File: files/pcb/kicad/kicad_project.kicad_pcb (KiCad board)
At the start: 2 copper layers, 100 x 96 mm, 113 parts, among them CON1 USB_MINI_B, IC1 ATMEGA328-A, IC10 FET, IC11 DS1307, IC12 LPS331AP, IC13 AM2321, IC2 IC_16PIN, IC3 IC_4PIN, IC4 IC_4PIN, IC5 SN74141_K155NA, IC6 TLP627-4, IC7 TLP627-4, IC8 MY_3_TERMINAL_REGULATOR, IC9 ICM7555CD, K1 CONN_3, K2 CONN_3, K3 CONN_3, K4 CONN_3, P1 CONN_6, SW1 SW_PUSH, SW2 EVQWK, SW3 SW_PUSH, SW4 SW_PUSH, SW5 SW_PUSH, T1 2SC, T2 2SC, T3 2SA, U1 NEON, U10 NIXIE_IN_16, U11 DC_JACK, U12 LOAD, U13 remocon, U14 napion, U15 MY_PIN52, U16 MY_PIN52, U17 MY_PIN52, U18 MY_PIN52, U2 NEON, U3 NEON, U4 NEON, U5 NIXIE_IN_16, U6 NIXIE_IN_16, U7 NIXIE_IN_16, U8 NIXIE_IN_16, U9 NIXIE_IN_16, X1 12MHz, X2 32.768kHz

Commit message: PCB更新
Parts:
- moved C13 111.8 mm to (350.4, 144.9)
- moved IC10 111.8 mm to (330.2, 146.7)
- moved IC9 111.8 mm to (318.6, 142.1)
- moved L1 111.8 mm to (340.8, 144.7)
- moved T1 111.8 mm to (313.6, 148.5)
- moved T2 111.8 mm to (318.6, 148.3)
- moved T3 111.8 mm to (323.6, 148.3)
- moved VR1 111.8 mm to (311.6, 142.1)
- moved VR2 111.8 mm to (307.8, 142.1)
- moved C14 8.81 mm to (197.8, 135.3)
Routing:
- net GND: track 268.3 -> 35.8 mm, vias 11 -> 0
- net /nixie/N0: track 199.0 -> 0.00 mm, vias 10 -> 0
- net /nixie/Sheet53F9F7BA/dot_cathode_l: track 197.8 -> 0.00 mm, vias 7 -> 0
- net /nixie/N1: track 184.7 -> 0.00 mm, vias 13 -> 0
- net /nixie/N2: track 180.0 -> 0.00 mm, vias 9 -> 0
- net GND_L: track 192.4 -> 14.7 mm, vias 8 -> 0
- net +5V: track 190.2 -> 15.3 mm, vias 11 -> 1
- net /nixie/Sheet53F9F7BA/dot_cathode_r: track 140.3 -> 0.00 mm, vias 5 -> 0
- net /nixie/N9: track 124.2 -> 0.00 mm, vias 3 -> 0
- net /nixie/N8: track 107.6 -> 0.00 mm, vias 4 -> 0
- net /nixie/N7: track 105.7 -> 0.00 mm, vias 5 -> 0
- net /nixie/N4: track 104.3 -> 0.00 mm, vias 3 -> 0
- net /nixie/N3: track 100.9 -> 0.00 mm, vias 3 -> 0
- net /nixie/N6: track 96.1 -> 0.00 mm, vias 6 -> 0
- net (no net): track 95.3 -> 0.00 mm, vias 3 -> 0
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
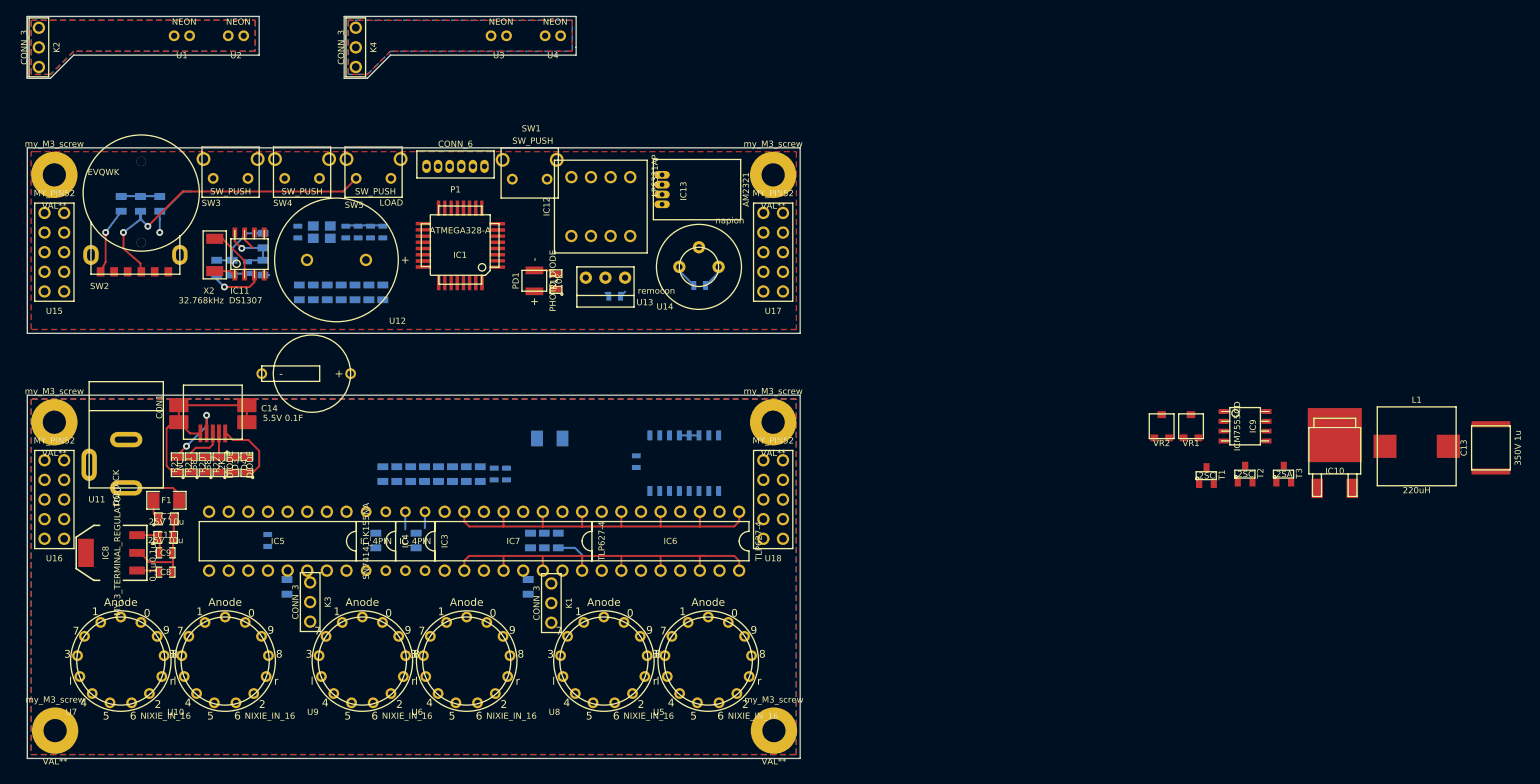
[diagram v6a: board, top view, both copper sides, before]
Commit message: 必要性の低い部品を削除
機能てんこ盛りよりシンプル小型化のほうがいいかなと思ったので一気に部品を削除
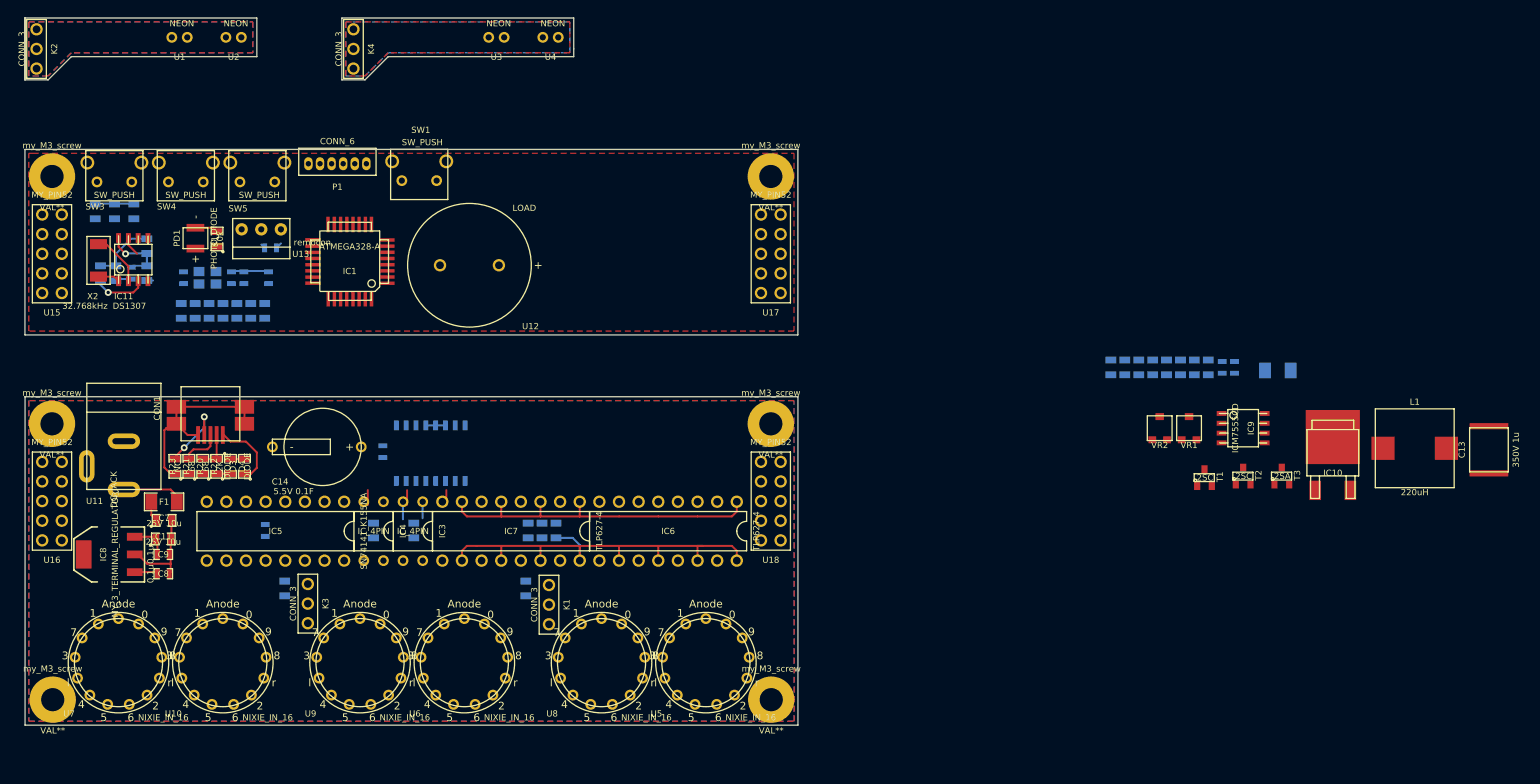
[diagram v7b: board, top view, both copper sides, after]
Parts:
- removed C17, C19: 0.1u, SM0603_Capa
- removed IC12: LPS331AP, my_dip_module
- removed IC13: AM2321, my_am2321
- removed SW2: EVQWK, my_rotary_switch
- removed U14: napion, my_napion
- moved C10 95.2 mm to (317.2, 134.5)
- moved R13 95.2 mm to (310.2, 134.5)
- moved R14 95.2 mm to (308.4, 134.5)
- moved R19 95.2 mm to (301.2, 134.5)
- moved C12 95.2 mm to (315.6, 134.5)
- moved R15 95.2 mm to (306.6, 134.5)
- moved R16 95.2 mm to (313.8, 134.5)
- moved R17 95.2 mm to (304.8, 134.5)
- moved R12 95.2 mm to (312.0, 134.5)
- moved R18 95.2 mm to (303.0, 134.5)
- moved D2 94.6 mm to (322.8, 134.9)
- moved U13 45.0 mm to (191.3, 118.9)
- moved C16 45.0 mm to (192.5, 119.0)
- moved PD1 44.2 mm to (182.8, 117.8)
- moved R11 44.2 mm to (185.6, 117.9)
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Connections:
- IC1 pad 2: /Sheet53F9209C/out -> (no net)
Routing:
- net /Sheet53F8FD69/Push: track 42.2 -> 0.00 mm, vias 2 -> 0
- net /Sheet53F8FD69/A: track 8.66 -> 0.00 mm, vias 1 -> 0
- net /Sheet53F8FD69/B: track 7.86 -> 0.00 mm, vias 1 -> 0
- net N-0000046: track 50.1 -> 44.3 mm
- net GND: track 35.8 -> 32.6 mm
- net +5V: track 15.3 -> 12.2 mm
- net /nixie/L8: track 0.00 -> 1.91 mm
- net /PB_P4: track 0.00 -> 1.91 mm
- net /PB_P3: track 1.96 -> 3.87 mm
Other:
- board size 100 x 96 mm -> 100 x 91.5 mm

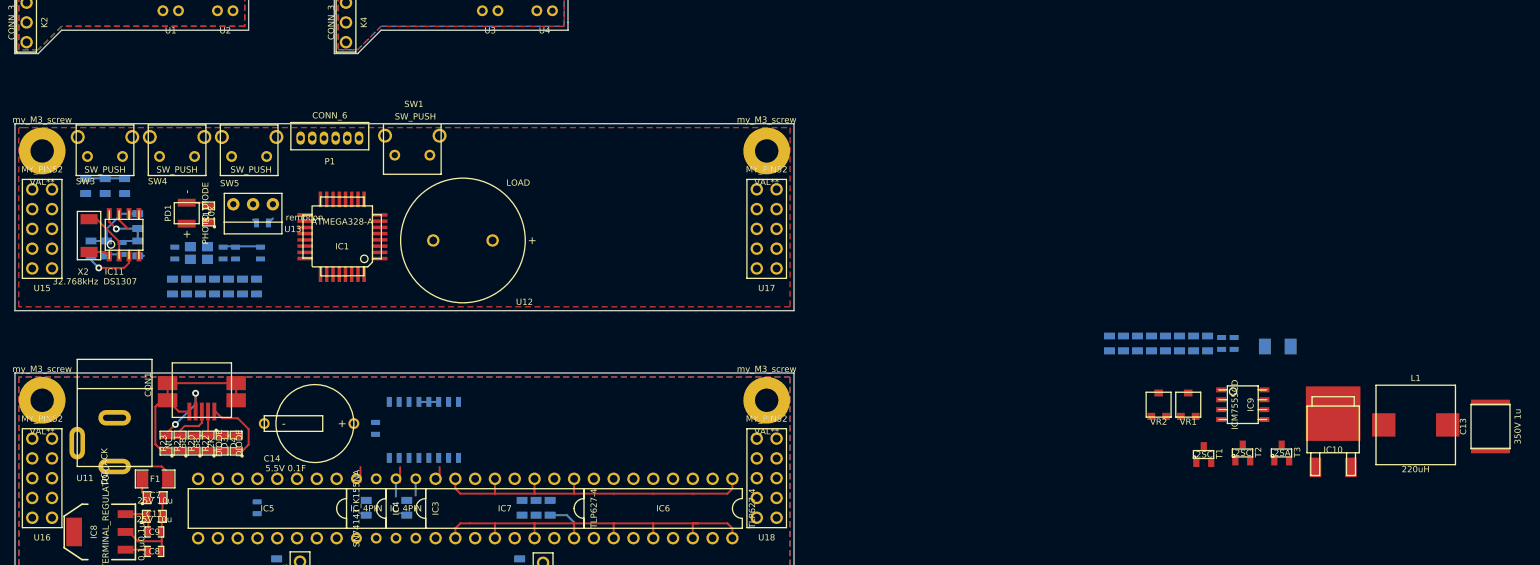
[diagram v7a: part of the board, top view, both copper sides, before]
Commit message: 設計見直し
部品見直し
USB・DCジャック自動切り替え
マイコンを下段のボードに移動
ニキシー管駆動電源を上段ボードに移動
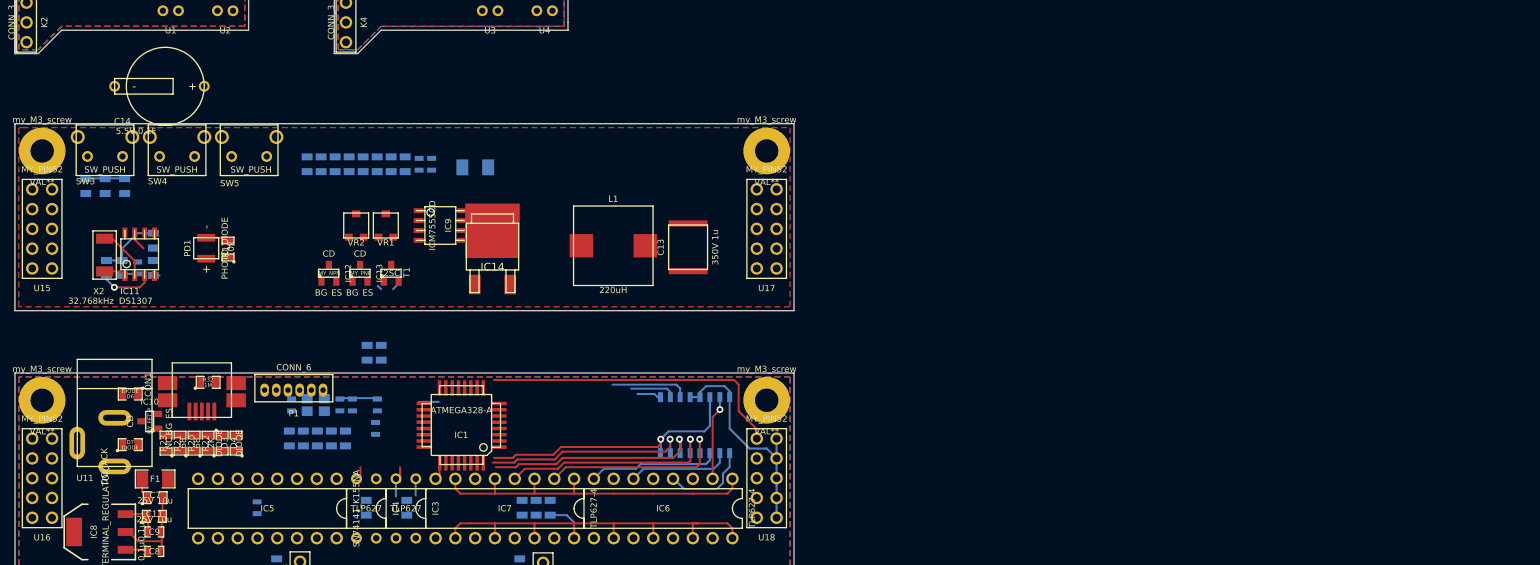
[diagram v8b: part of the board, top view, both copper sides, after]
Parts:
- removed C16: 0.1u, SM0603_Capa
- removed SW1: SW_PUSH, my_tact_switch
- removed T2: 2SC, SOT23
- removed T3: 2SA, SOT23
- removed U12: LOAD, my_sounder
- removed U13: remocon, my_remocon
- added D6: DIODE, SM0805, F.Cu at (175.5, 141.0)
- added D7: DIODE, SM0805, F.Cu at (175.5, 147.5)
- added IC12: MY_NPN, my_SOT23, F.Cu at (201.0, 125.5)
- added IC13: MY_PNP, my_SOT23, F.Cu at (205.0, 125.5)
- added IC14: MY_FET_N, my_sot428, F.Cu at (222.0, 123.5)
- added R32: 1M, SM0805, F.Cu at (185.5, 139.5)
- IC10: value FET -> MY_FET_P; footprint my_sot428 -> my_SOT23
- IC2: value IC_16PIN -> 74LC138
- IC3, IC4: value IC_4PIN -> TLP627
- moved IC10 151.9 mm to (178.0, 144.5), turned to 90 degrees
- moved T1 106.9 mm to (209.0, 125.5)
- moved C10 105.5 mm to (214.2, 111.5)
- moved R13 105.5 mm to (207.2, 111.5)
- moved R14 105.5 mm to (205.4, 111.5)
- moved R19 105.5 mm to (198.2, 111.5)
- moved C12 105.5 mm to (212.6, 111.5)
- moved C13 105.5 mm to (247.1, 122.2)
- moved D2 105.5 mm to (219.8, 111.9)
- moved R15 105.5 mm to (203.6, 111.5)
- moved R16 105.5 mm to (210.8, 111.5)
- moved R17 105.5 mm to (201.8, 111.5)
- moved IC9 105.5 mm to (215.3, 119.4)
- moved L1 105.5 mm to (237.5, 122.0)
- moved R12 105.5 mm to (209.0, 111.5)
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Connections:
- net /Sheet53F91D14/beep renamed /SCK
- C10 pad 1: GND_L -> PINGND
- C10 pad 2: N-0000078 -> PIN9V
- C11 pad 1: 5V_L -> +5V
- C11 pad 2: GND_L -> GND
- C12 pad 2: GND_L -> PINGND
- C13 pad 2: GND_L -> PINGND
- C14 pad 1: CLK_PW_L -> N-00000108
- C14 pad 2: GND -> PINGND
- C15 pad 2: GND_L -> GND
- C18 pad 1: +5V -> PIN5V
- C18 pad 2: GND -> PINGND
- C6 pad 1: GND_L -> GND
- C7 pad 1: N-0000078 -> N-0000087
- C7 pad 2: GND_L -> GND
- C8 pad 1: N-0000078 -> N-0000087
- C8 pad 2: GND_L -> GND
- C9 pad 1: 5V_L -> +5V
- C9 pad 2: GND_L -> GND
- CON1 pad 1: N-0000083 -> USB5V
- CON1 pad 2: N-0000085 -> N-00000105
- CON1 pad 3: N-0000087 -> N-00000104
- D2 pad 1: N-0000073 -> N-0000088
- D3 pad 1: N-0000084 -> GND
- D3 pad 2: +5V -> N-00000104
- D4 pad 1: N-0000083 -> GND
- D4 pad 2: N-0000084 -> N-00000105
- D5 pad 2: CLK_PW_H -> N-00000108
- F1 pad 2: N-0000078 -> N-0000087
- IC1 pad 10: /Sheet53F8FD69/B -> /PD6
- IC1 pad 11: /Sheet53F8FD69/Push -> /PD7
- IC1 pad 19: /Sheet53F8BA4D/out -> /ADC6
- IC1 pad 2: (no net) -> /PD4
- IC1 pad 27: /Sheet53F905A8/SCL -> /SDA
- IC1 pad 28: /Sheet53F905A8/SDA -> /SCL
- IC1 pad 30: /Sheet53F905A8/CLKOUT -> (no net)
- IC1 pad 31: /Sheet53F9209A/out -> (no net)
- IC1 pad 9: /Sheet53F8FD69/A -> /PD5
- IC10 pad 1: N-0000071 -> N-0000095
- IC10 pad 2: N-0000073 -> USB5V
- IC10 pad 3: GND_L -> N-0000093
- IC11 pad 3: CLK_PW_H -> N-00000108
- IC11 pad 4: GND -> PINGND
- IC11 pad 5: /Sheet53F905A8/SDA -> PINSDA
- IC11 pad 6: /Sheet53F905A8/SCL -> PINSCL
- IC11 pad 7: /Sheet53F905A8/CLKOUT -> PINCLKOUT
- IC11 pad 8: +5V -> PIN5V
- IC2 pad 1: /PB_P0 -> /PB0
- IC2 pad 2: /PB_P1 -> /PB1
- IC2 pad 3: /PB_P2 -> /PB2
- IC2 pad 4: GND_L -> GND
- IC2 pad 5: GND_L -> GND
- IC2 pad 6: GND_L -> +5V
- IC2 pad 8: GND_L -> GND
- IC3 pad 2: /PB_P3 -> /MOSI
- IC4 pad 2: /PB_P4 -> /MISO
- IC5 pad 12: GND_L -> GND
- IC5 pad 3: /PC_P3 -> /PC3
- IC5 pad 4: /PC_P2 -> /PC2
- IC5 pad 6: /PC_P1 -> /PC1
- IC5 pad 7: /PC_P0 -> /PC0
- IC8 pad 1: N-0000078 -> N-0000087
- IC8 pad 2: GND_L -> GND
- IC8 pad 3: 5V_L -> +5V
- IC9 pad 1: GND_L -> PINGND
- IC9 pad 4: N-0000078 -> PIN9V
- IC9 pad 8: N-0000078 -> PIN9V
- L1 pad 1: N-0000078 -> PIN9V
- L1 pad 2: N-0000073 -> N-0000088
- PD1 pad 1: +5V -> PIN5V
- PD1 pad 2: /Sheet53F8BA4D/out -> PINADC6
- R10 pad 2: GND_L -> GND
- R11 pad 1: GND -> PINGND
- R11 pad 2: /Sheet53F8BA4D/out -> PINADC6
- R12 pad 2: N-0000078 -> PIN9V
- R15 pad 1: N-0000071 -> N-0000099
- R16 pad 1: N-0000078 -> PIN9V
- R20 pad 2: N-0000085 -> N-00000105
- R21 pad 2: N-0000087 -> N-00000104
- R22 pad 2: N-0000085 -> N-00000105
- R24 pad 1: +5V -> PIN5V
- R24 pad 2: /Sheet53F8FD69/A -> PINPD5
- R25 pad 1: +5V -> PIN5V
- R25 pad 2: /Sheet53F8FD69/B -> PINPD6
- R26 pad 1: +5V -> PIN5V
- R26 pad 2: /Sheet53F8FD69/Push -> PINPD7
- R27 pad 1: 5V_L -> PIN5V
- R28 pad 2: GND -> PINGND
- R29 pad 1: +5V -> PIN5V
- R29 pad 2: /Sheet53F905A8/CLKOUT -> PINCLKOUT
- R30 pad 2: GND_L -> GND
- R31 pad 2: GND_L -> GND
- R4 pad 2: /Sheet53F905A8/SCL -> /SCL
- R5 pad 2: /Sheet53F905A8/SDA -> /SDA
- R8 pad 1: 170V -> PIN170V
- R9 pad 2: GND_L -> GND
- SW3 pad 1: /Sheet53F8FD69/A -> PINPD5
- SW3 pad 2: GND -> PINGND
- SW4 pad 1: /Sheet53F8FD69/B -> PINPD6
- SW4 pad 2: GND -> PINGND
- SW5 pad 1: /Sheet53F8FD69/Push -> PINPD7
- SW5 pad 2: GND -> PINGND
- T1 pad 3: GND_L -> PINGND
- U11 pad 1: +9V -> N-0000095
- U11 pad 3: GND_L -> GND
- U15 pad 1: CLK_PW_H -> PINPD5
- U15 pad 10: +5V -> PIN5V
- U15 pad 2: GND -> PINPD6
- U15 pad 3: GND -> PINPD7
- U15 pad 4: GND -> (no net)
- U15 pad 5: GND -> PINGND
- U15 pad 6: /PC3 -> PINSCL
- U15 pad 7: /PC2 -> PINSDA
- U15 pad 8: /PC1 -> PINCLKOUT
- U15 pad 9: /PC0 -> PINADC6
- U16 pad 1: CLK_PW_L -> /PD5
- U16 pad 10: 5V_L -> +5V
- U16 pad 2: GND_L -> /PD6
- U16 pad 3: GND_L -> /PD7
- U16 pad 4: GND_L -> (no net)
- U16 pad 5: GND_L -> GND
- U16 pad 6: /PC_P3 -> /SCL
- U16 pad 7: /PC_P2 -> /SDA
- U16 pad 8: /PC_P1 -> /PD4
- U16 pad 9: /PC_P0 -> /ADC6
- U17 pad 1: /PB0 -> PIN9V
- U17 pad 10: GND -> (no net)
- U17 pad 2: /PB1 -> (no net)
- U17 pad 3: /PB2 -> (no net)
- U17 pad 4: /MOSI -> (no net)
- U17 pad 5: /MISO -> 170V
- U17 pad 6: GND -> PINGND
- U17 pad 7: GND -> (no net)
- U17 pad 8: GND -> (no net)
- U17 pad 9: GND -> (no net)
- U18 pad 1: /PB_P0 -> +9V
- U18 pad 10: GND_L -> GND
- U18 pad 2: /PB_P1 -> (no net)
- U18 pad 3: /PB_P2 -> (no net)
- U18 pad 4: /PB_P3 -> (no net)
- U18 pad 5: /PB_P4 -> PIN170V
- U18 pad 6: GND_L -> GND
- U18 pad 7: GND_L -> GND
- U18 pad 8: GND_L -> GND
- U18 pad 9: GND_L -> GND
- VR2 pad 2: GND_L -> PINGND
- VR2 pad 3: GND_L -> PINGND
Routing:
- net +9V: track 7.98 -> 39.5 mm
- net /nixie/L6: track 0.00 -> 28.1 mm, vias 0 -> 1
- net /nixie/L7: track 0.00 -> 28.0 mm, vias 0 -> 1
- net +5V: track 12.2 -> 40.2 mm
- net /nixie/L8: track 1.91 -> 28.3 mm, vias 0 -> 1
- net /nixie/L5: track 0.00 -> 24.5 mm, vias 0 -> 1
- net /nixie/L4: track 0.00 -> 16.8 mm
- net GND_L: track 14.7 -> 0.00 mm
- net GND: track 32.6 -> 45.8 mm
- net /nixie/L3: track 0.00 -> 13.2 mm
- net /nixie/L2: track 0.00 -> 11.5 mm
- net /nixie/L1: track 0.00 -> 10.9 mm, vias 0 -> 1
- net /PB2: track 0.00 -> 10.0 mm
- net N-00000103: track 9.37 -> 0.00 mm, vias 2 -> 0
- net N-0000083: track 9.24 -> 0.00 mm
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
